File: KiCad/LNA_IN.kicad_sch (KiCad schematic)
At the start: 6 parts

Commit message: Reset all annotationss
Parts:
- renumbered AE2 to AE1, C11 to C15, C12 to C16, C13 to C17, L5 to L2, L6 to L3
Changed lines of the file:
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@@
 		(dnp no)
 		(fields_autoplaced yes)
-		(property "Reference" "C13"
+		(property "Reference" "C17"
 			(at 161.29 106.6799 0)
 			(effects
@@
 			(project "Senior Project"
 				(path "/16f8cce7-467e-4342-b55a-00af81cd6f69/b83b2aad-ec0d-4434-a2c8-9afe2bddf11d"
-					(reference "C13")
+					(reference "C17")
 					(unit 1)
 				)
@@
 		(dnp no)
 		(fields_autoplaced yes)
-		(property "Reference" "C11"
+		(property "Reference" "C15"
 			(at 140.97 96.5199 0)
 			(effects
@@
 			(project "Senior Project"
 				(path "/16f8cce7-467e-4342-b55a-00af81cd6f69/b83b2aad-ec0d-4434-a2c8-9afe2bddf11d"
-					(reference "C11")
+					(reference "C15")
 					(unit 1)
 				)
@@
 		(dnp no)
 		(fields_autoplaced yes)
-		(property "Reference" "#PWR021"
+		(property "Reference" "#PWR029"
 			(at 137.16 110.49 0)
 			(effects
@@
 			(project "Senior Project"
 				(path "/16f8cce7-467e-4342-b55a-00af81cd6f69/b83b2aad-ec0d-4434-a2c8-9afe2bddf11d"
-					(reference "#PWR021")
+					(reference "#PWR029")
 					(unit 1)
 				)
@@
 		(dnp no)
 		(fields_autoplaced yes)
-		(property "Reference" "#PWR024"
+		(property "Reference" "#PWR032"
 			(at 161.29 105.41 0)
 			(effects
@@
 			(project "Senior Project"
 				(path "/16f8cce7-467e-4342-b55a-00af81cd6f69/b83b2aad-ec0d-4434-a2c8-9afe2bddf11d"
-					(reference "#PWR024")
+					(reference "#PWR032")
 					(unit 1)
 				)
@@
 		(dnp no)
 		(fields_autoplaced yes)
-		(property "Reference" "AE2"
+		(property "Reference" "AE1"
 			(at 172.72 93.2814 90)
 			(effects
@@
 			(project "Senior Project"
 				(path "/16f8cce7-467e-4342-b55a-00af81cd6f69/b83b2aad-ec0d-4434-a2c8-9afe2bddf11d"
-					(reference "AE2")
+					(reference "AE1")
 					(unit 1)
 				)
@@
 		(dnp no)
 		(fields_autoplaced yes)
-		(property "Reference" "C12"
+		(property "Reference" "C16"
 			(at 151.13 96.5199 0)
 			(effects
@@
 			(project "Senior Project"
 				(path "/16f8cce7-467e-4342-b55a-00af81cd6f69/b83b2aad-ec0d-4434-a2c8-9afe2bddf11d"
-					(reference "C12")
+					(reference "C16")
 					(unit 1)
 				)
@@
 		(dnp no)
 		(fields_autoplaced yes)
-		(property "Reference" "#PWR022"
+		(property "Reference" "#PWR030"
 			(at 147.32 110.49 0)
 			(effects
@@
 			(project "Senior Project"
 				(path "/16f8cce7-467e-4342-b55a-00af81cd6f69/b83b2aad-ec0d-4434-a2c8-9afe2bddf11d"
-					(reference "#PWR022")
+					(reference "#PWR030")
 					(unit 1)
 				)
@@
 		(dnp no)
 		(fields_autoplaced yes)
-		(property "Reference" "#PWR023"
+		(property "Reference" "#PWR031"
 			(at 157.48 120.65 0)
 			(effects
@@
 			(project "Senior Project"
 				(path "/16f8cce7-467e-4342-b55a-00af81cd6f69/b83b2aad-ec0d-4434-a2c8-9afe2bddf11d"
-					(reference "#PWR023")
+					(reference "#PWR031")
 					(unit 1)
 				)
@@
 		(dnp no)
 		(fields_autoplaced yes)
-		(property "Reference" "L6"
+		(property "Reference" "L3"
 			(at 158.75 96.5199 0)
 			(effects
@@
 			(project "Senior Project"
 				(path "/16f8cce7-467e-4342-b55a-00af81cd6f69/b83b2aad-ec0d-4434-a2c8-9afe2bddf11d"
-					(reference "L6")
+					(reference "L3")
 					(unit 1)
 				)
@@
 		(dnp no)
 		(fields_autoplaced yes)
-		(property "Reference" "L5"
+		(property "Reference" "L2"
 			(at 142.24 88.9 90)
 			(effects
@@
 			(project "Senior Project"
 				(path "/16f8cce7-467e-4342-b55a-00af81cd6f69/b83b2aad-ec0d-4434-a2c8-9afe2bddf11d"
-					(reference "L5")
-					(unit 1)
-				)
+					(reference "L2")
+					(unit 1)
+				)

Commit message: Updated several footprints
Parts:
- AE1: footprint (none) -> RF_Antenna:Molex_47948-0001_2.4Ghz
- C15, C16, C17: footprint (none) -> Capacitor_SMD:C_0402_1005Metric
- L2, L3: footprint (none) -> Inductor_SMD:L_0402_1005Metric
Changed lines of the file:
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@@
 			)
 		)
-		(property "Footprint" ""
+		(property "Footprint" "Capacitor_SMD:C_0402_1005Metric"
 			(at 158.4452 111.76 0)
 			(effects
@@
 			)
 		)
-		(property "Footprint" ""
+		(property "Footprint" "Capacitor_SMD:C_0402_1005Metric"
 			(at 138.1252 101.6 0)
 			(effects
@@
 			)
 		)
-		(property "Footprint" ""
+		(property "Footprint" "RF_Antenna:Molex_47948-0001_2.4Ghz"
 			(at 168.91 93.98 0)
 			(effects
@@
 			)
 		)
-		(property "Footprint" ""
+		(property "Footprint" "Capacitor_SMD:C_0402_1005Metric"
 			(at 148.2852 101.6 0)
 			(effects
@@
 			)
 		)
-		(property "Footprint" ""
+		(property "Footprint" "Inductor_SMD:L_0402_1005Metric"
 			(at 157.48 97.79 0)
 			(effects
@@
 			)
 		)
-		(property "Footprint" ""
+		(property "Footprint" "Inductor_SMD:L_0402_1005Metric"
 			(at 142.24 93.98 0)
 			(effects

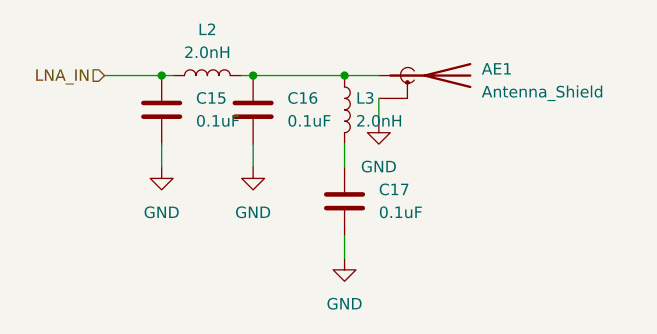
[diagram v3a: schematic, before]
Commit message: tighten up layout, swap out USB connector
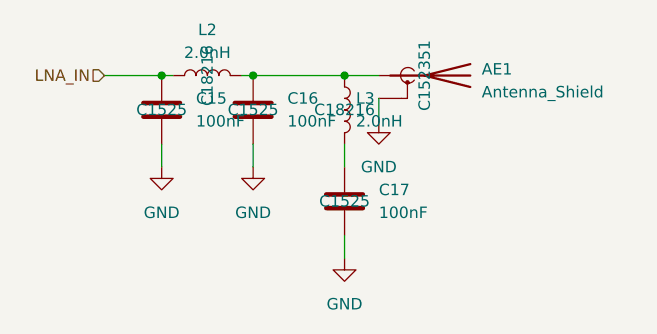
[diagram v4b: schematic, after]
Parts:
- AE1: LCSC (none) -> C152351
- C15, C16, C17: value 0.1uF -> 100nF; LCSC (none) -> C1525
- L2, L3: LCSC (none) -> C18216
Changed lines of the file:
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@@
 			)
 		)
-		(property "Value" "0.1uF"
+		(property "Value" "100nF"
 			(at 161.29 109.2199 0)
 			(effects
@@
 			)
 		)
+		(property "LCSC" "C1525"
+			(at 157.48 107.95 0)
+			(effects
+				(font
+					(size 1.27 1.27)
+				)
+			)
+		)
 		(pin "1"
 		)
@@
 			)
 		)
-		(property "Value" "0.1uF"
+		(property "Value" "100nF"
 			(at 140.97 99.0599 0)
 			(effects
@@
 			)
 		)
+		(property "LCSC" "C1525"
+			(at 137.16 97.79 0)
+			(effects
+				(font
+					(size 1.27 1.27)
+				)
+			)
+		)
 		(pin "1"
 		)
@@
 			)
 		)
+		(property "LCSC" "C152351"
+			(at 166.37 93.98 0)
+			(effects
+				(font
+					(size 1.27 1.27)
+				)
+			)
+		)
 		(pin "1"
 		)
@@
 			)
 		)
-		(property "Value" "0.1uF"
+		(property "Value" "100nF"
 			(at 151.13 99.0599 0)
 			(effects
@@
 			)
 		)
+		(property "LCSC" "C1525"
+			(at 147.32 97.79 0)
+			(effects
+				(font
+					(size 1.27 1.27)
+				)
+			)
+		)
 		(pin "1"
 		)
@@
 			)
 		)
+		(property "LCSC" "C18216"
+			(at 157.48 97.79 0)
+			(effects
+				(font
+					(size 1.27 1.27)
+				)
+			)
+		)
 		(pin "1"
 		)
@@
 			)
 		)
+		(property "LCSC" "C18216"
+			(at 142.24 93.98 0)
+			(effects
+				(font
+					(size 1.27 1.27)
+				)
+			)
+		)
